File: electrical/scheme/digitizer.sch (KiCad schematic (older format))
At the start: 43 parts

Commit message: a
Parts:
- added C? (x2): 4u7, symbol C
- added C?: 3u9, symbol C
- added C? (x4): 100n, symbol C
- added R?: 100 5%, symbol R
- added R? (x2): 16 5%, symbol R
- added U?: AD7683, symbol AD7683
- added U?: MCP1703T-3302E/CB, symbol MCP1703T-3302E/CB
- added U?: AD8610, symbol AD8610
- added U?: ADG5204, symbol ADG5204
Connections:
- net labels added: adc_cs, mux-0, mux-1, src01, src02, src03, src04, vref
- wire segments 173 -> 230
- no-connect marks 5 -> 13
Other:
- moved on the sheet: C?, D?, L?, R?, U?, stm32?

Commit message: a
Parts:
- added C?: 100n, symbol C
- added C?: 1n, symbol C
- added C? (x3): 4u7, symbol C
- added C?: 10n, symbol C
- added R? (x4): 16 5%, symbol R
- added U?: MCP1703T-3302E/CB, symbol MCP1703T-3302E/CB
- R?: value 100 5% -> 50 5%
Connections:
- net labels added: adc-ref, bias-ref, in01, in02, in03, in04
- net labels removed: vref
- wire segments 230 -> 278
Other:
- moved on the sheet: C?, R?, U?

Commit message: a.
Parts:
- removed C? (x2): 100n, symbol C
- removed C? (x2): 4u7, symbol C
- removed C?: 10n, symbol C
- removed K?: swd, symbol CONN_3
- removed R? (x6): 16 5%, symbol R
- removed U?: AD8610, symbol AD8610
- removed U?: MCP1703T-3302E/CB, symbol MCP1703T-3302E/CB
- added C? (x9): 100n, symbol C
- added C? (x3): 4u7, symbol C
- added C? (x2): 1n, symbol C
- added D? (x2): LED, symbol LED
- added P?: in-0, symbol BNC
- added P?: in-1, symbol BNC
- added P?: in-2, symbol BNC
- added P?: in-3, symbol BNC
- added P?: mode, symbol CONN_01X02
- added P?: swd, symbol CONN_01X03
- added P?: ~rst~, symbol CONN_01X01
- added P?: out-0, symbol BNC
- added P?: out-1, symbol BNC
- added P?: ext, symbol CONN_01X13
- added P?: trig, symbol BNC
- added P?: trig-mode, symbol CONN_01X03
- added R? (x5): 10k 5%, symbol R
- added R?: 13k 5%, symbol R
- added R?: 1k5 5%, symbol R
- added R? (x6): 16 5%, symbol R
- added R?: 120k 5%, symbol R
- added R? (x2): 8k2 5%, symbol R
- added R? (x2): 1 5%, symbol R
- added R? (x2): 1k6 5%, symbol R
- added R? (x2): 3k3 5%, symbol R
- added R? (x2): 12k 5%, symbol R
- added R? (x3): 1k 5%, symbol R
- added U? (x6): AD8620, symbol AD8620
- added U?: MCP1703T-3302E/CB, symbol MCP1703T-3302E/CB
- added U?: BAT54S, symbol BAT54S
- C? (x2): value C -> 18p
- C?: value 3u9 -> 3n
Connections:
- net labels added: adc-mux-0, adc-mux-1, dac-cs-0, dac-cs-1, dac-cs-2, dac-cs-3, dac-mosi, dac-ref, dac-sck, gpio-0, gpio-1, gpio-2, gpio-3, gpio-4, led-0, led-1, rx-2, src-0, src-1, src-2, src-3, tx-2
- net labels removed: bias-ref, mux-0, mux-1, src01, src02, src03, src04
- wire segments 278 -> 434
- no-connect marks 13 -> 10
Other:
- note added: "To eliminate uncertanity \nif input is high Z."
- moved on the sheet: C?, R?, U?

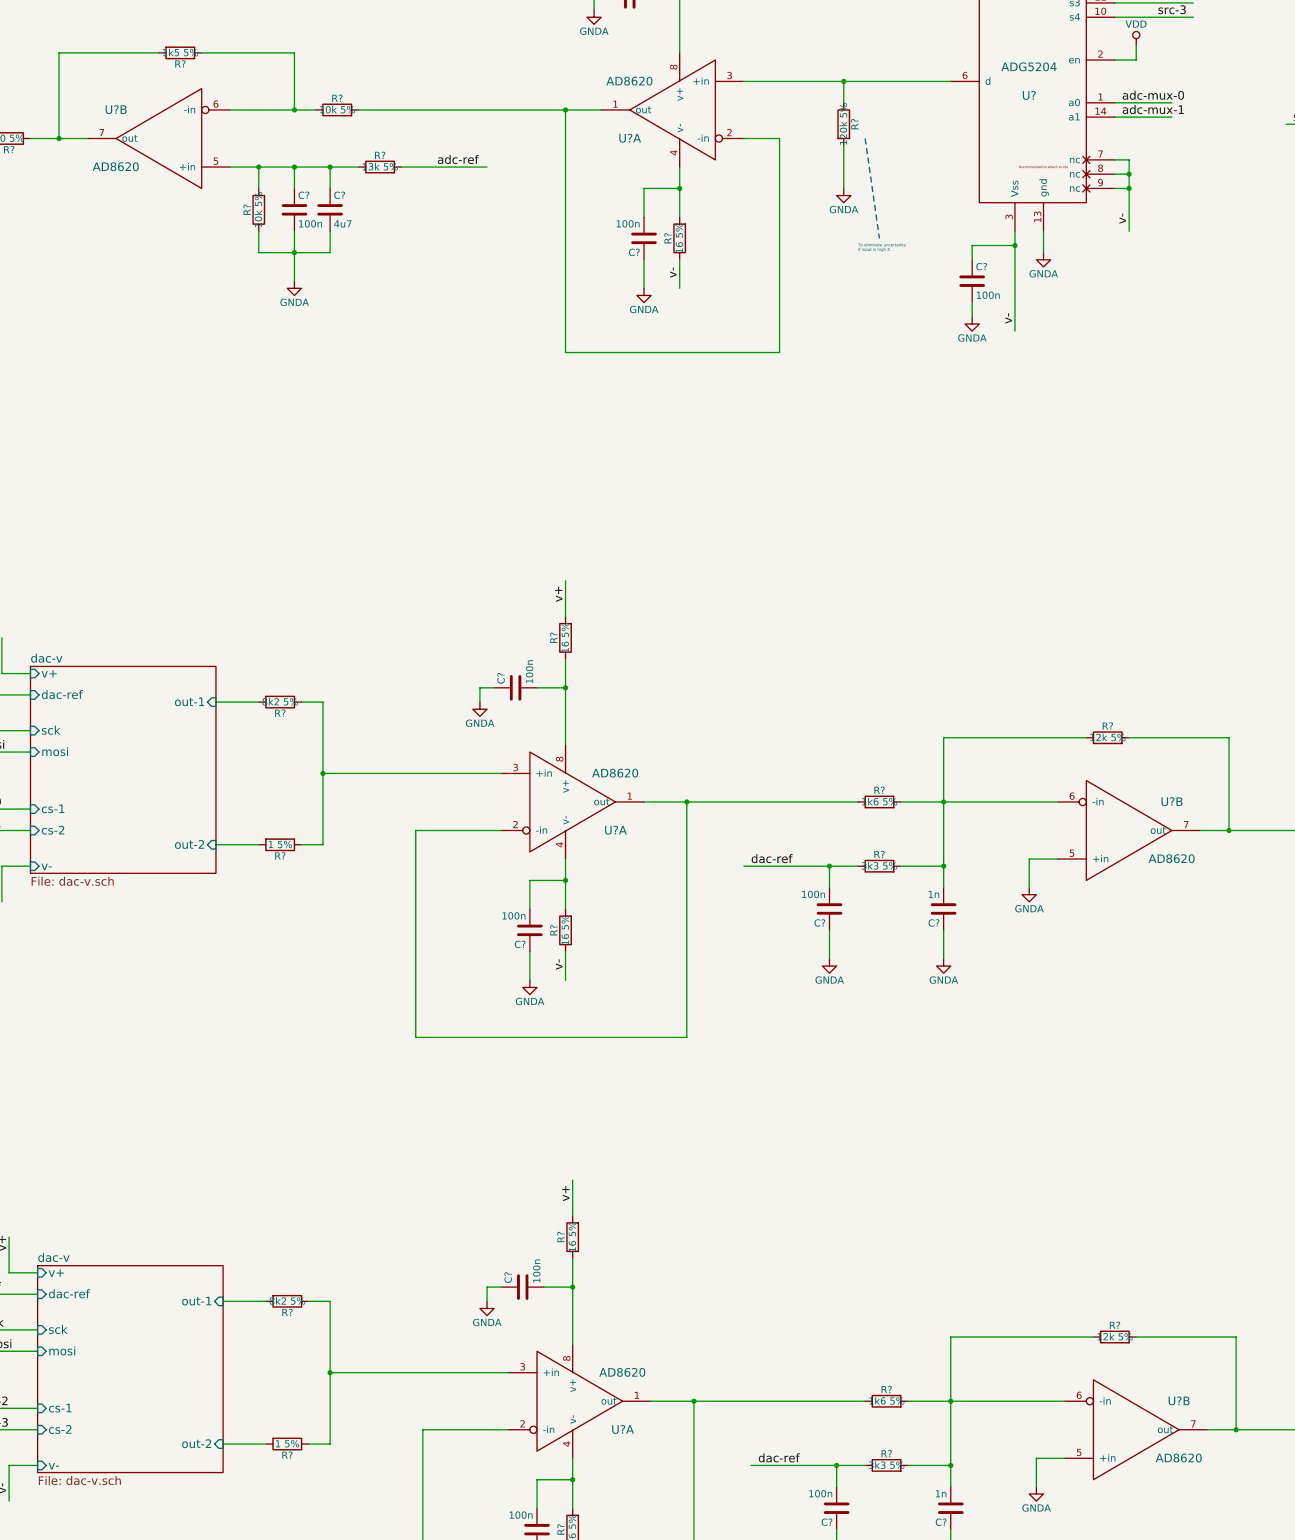
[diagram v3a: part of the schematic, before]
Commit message: Annotated opamps.
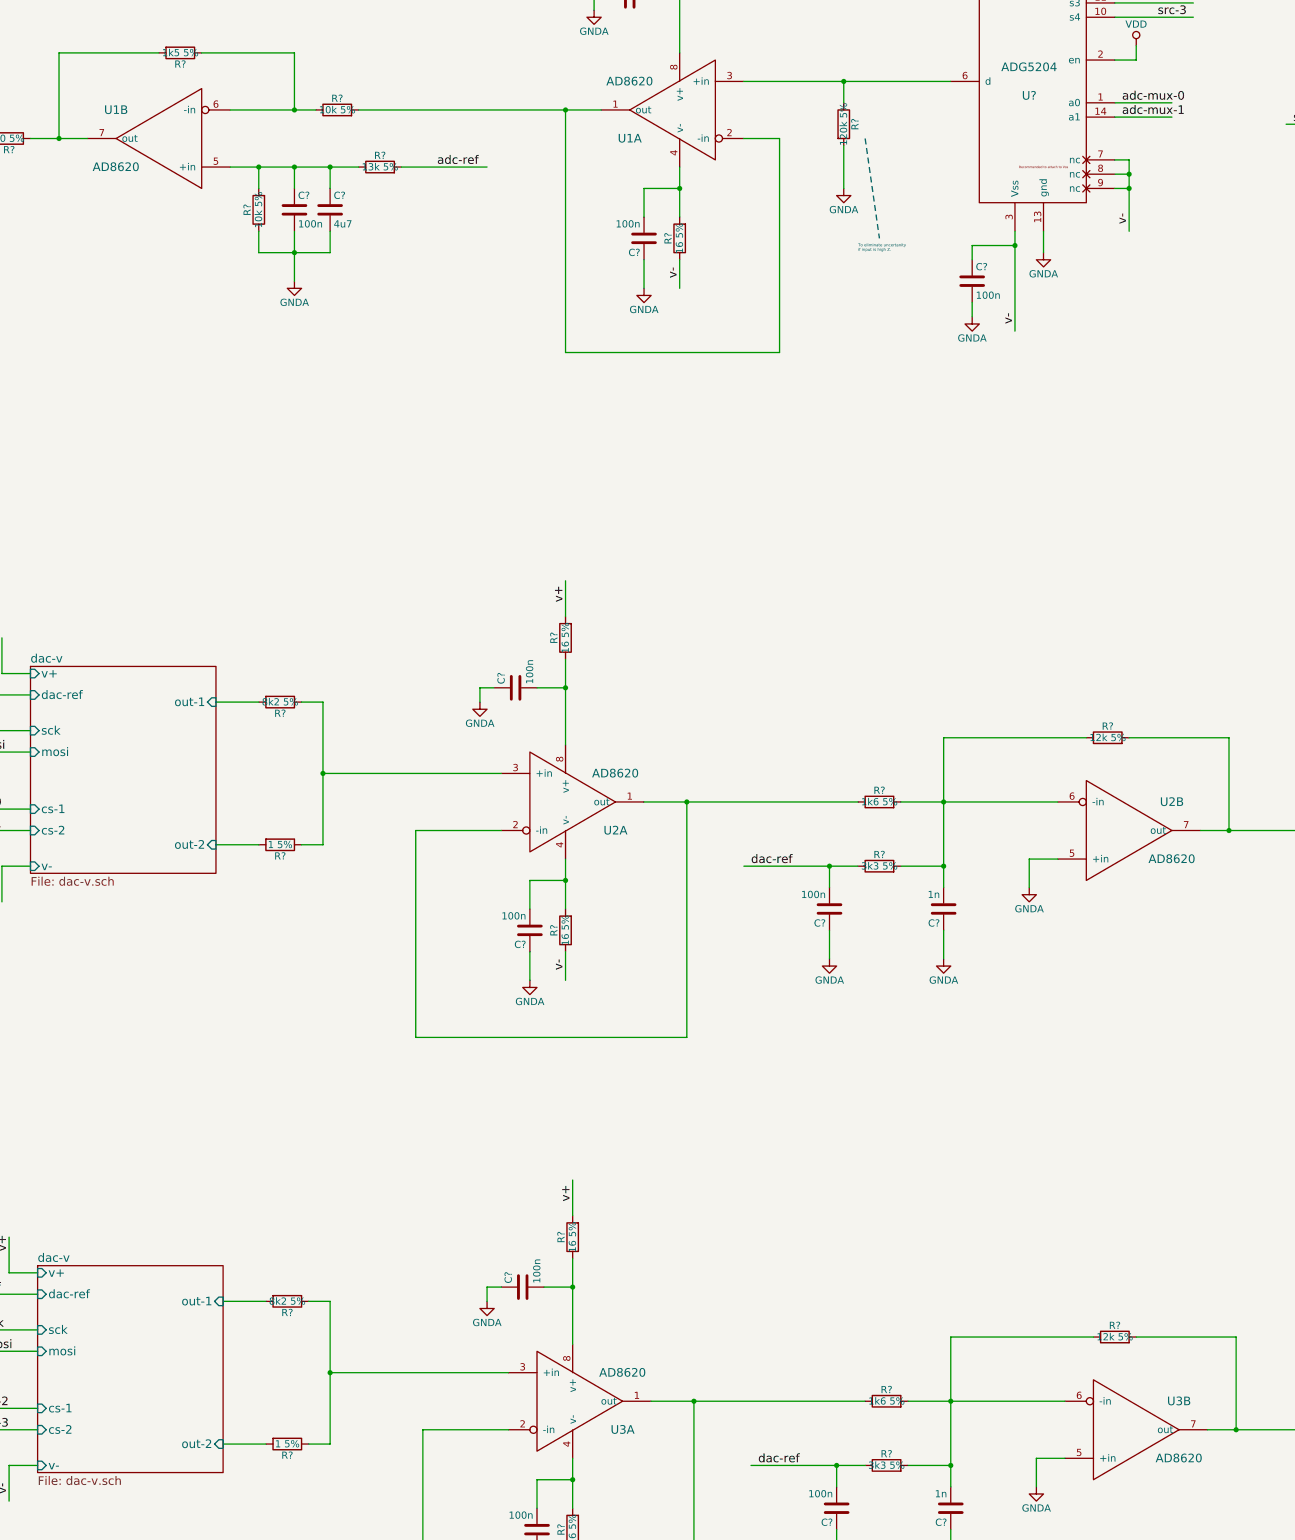
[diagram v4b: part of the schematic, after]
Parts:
- gave numbers to parts that had none: 3
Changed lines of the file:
@@
 	20300 2400 21750 2400
 $Comp
-L AD8620 U?
+L AD8620 U1
 U 1 1 5599DB58
 P 19850 2600
-F 0 "U?" H 20200 2400 60  0000 C CNN
+F 0 "U1" H 20200 2400 60  0000 C CNN
 F 1 "AD8620" H 20200 2800 60  0000 C CNN
 F 2 "" H 19900 2600 60  0000 C CNN
@@
 $EndComp
 $Comp
-L AD8620 U?
+L AD8620 U1
 U 2 1 5599DC7C
 P 16250 2800
-F 0 "U?" H 16600 2600 60  0000 C CNN
+F 0 "U1" H 16600 2600 60  0000 C CNN
 F 1 "AD8620" H 16600 3000 60  0000 C CNN
 F 2 "" H 16300 2800 60  0000 C CNN
@@
 	16900 7750 16600 7750
 $Comp
-L AD8620 U?
+L AD8620 U2
 U 1 1 55A17217
 P 19050 7450
-F 0 "U?" H 19400 7250 60  0000 C CNN
+F 0 "U2" H 19400 7250 60  0000 C CNN
 F 1 "AD8620" H 19400 7650 60  0000 C CNN
 F 2 "" H 19100 7450 60  0000 C CNN
@@
 Connection ~ 19900 7450
 $Comp
-L AD8620 U?
+L AD8620 U2
 U 2 1 55A2A22C
 P 22950 7650
-F 0 "U?" H 23300 7450 60  0000 C CNN
+F 0 "U2" H 23300 7450 60  0000 C CNN
 F 1 "AD8620" H 23300 7850 60  0000 C CNN
 F 2 "" H 23000 7650 60  0000 C CNN
@@
 	16950 11950 16650 11950
 $Comp
-L AD8620 U?
+L AD8620 U3
 U 1 1 55A5B81D
 P 19100 11650
-F 0 "U?" H 19450 11450 60  0000 C CNN
+F 0 "U3" H 19450 11450 60  0000 C CNN
 F 1 "AD8620" H 19450 11850 60  0000 C CNN
 F 2 "" H 19150 11650 60  0000 C CNN
@@
 Connection ~ 19950 11650
 $Comp
-L AD8620 U?
+L AD8620 U3
 U 2 1 55A5B860
 P 23000 11850
-F 0 "U?" H 23350 11650 60  0000 C CNN
+F 0 "U3" H 23350 11650 60  0000 C CNN
 F 1 "AD8620" H 23350 12050 60  0000 C CNN
 F 2 "" H 23050 11850 60  0000 C CNN

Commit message: a
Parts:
- removed P?: in-1, symbol BNC
- removed P?: in-2, symbol BNC
- removed P?: in-3, symbol BNC
- added C80, C81, C82, C83: 100n, Capacitors_SMD:C_0805_HandSoldering, symbol C
- added P10: in-2, Sockets_BNC:BNC_Socket_TYCO-AMP_LargePads, symbol BNC
- added P11: in-3, Sockets_BNC:BNC_Socket_TYCO-AMP_LargePads, symbol BNC
- added P12: in-1, Sockets_BNC:BNC_Socket_TYCO-AMP_LargePads, symbol BNC
- added R71, R72, R73, R74: 16 5%, Resistors_SMD:R_0805_HandSoldering, symbol R
- added U100, U101: AD8672, Housings_SOIC:SOIC-8_3.9x4.9mm_Pitch1.27mm, symbol AD8620
- C1, C10, C11, C12, C13, C14, C15, C16, C17, C18, C19, C2, C20, C21, C22, C23, C24, C25, C26, C28, C29, C3, C30, C31, C32, C33, C34, C35, C36, C37, C38, C4, C5, C6, C7, C8, C9: renamed from C?; footprint (none) -> Capacitors_SMD:C_0805_HandSoldering
- C27, C39: renamed from C?; footprint (none) -> Capacitors_ThroughHole:C_Radial_D10_L20_P5
- D1, D2: renamed from D?; footprint (none) -> LEDs:LED-3MM
- D3, D4: renamed from D?; footprint (none) -> Diodes_ThroughHole:Diode_DO-41_SOD81_Horizontal_RM10
- L1, L2: renamed from L?; footprint (none) -> my-lib:my_inductance
- P1: renamed from P?; footprint (none) -> Pin_Headers:Pin_Header_Straight_1x02
- P2: renamed from P?; footprint (none) -> Pin_Headers:Pin_Header_Straight_1x01
- P3: renamed from P?; footprint (none) -> Socket_Strips:Socket_Strip_Angled_1x13
- P4, P7, P8, P9: renamed from P?; footprint (none) -> Sockets_BNC:BNC_Socket_TYCO-AMP_LargePads
- P5: renamed from P?; footprint (none) -> Pin_Headers:Pin_Header_Angled_1x03
- P6: renamed from P?; footprint (none) -> Socket_Strips:Socket_Strip_Angled_1x03
- R1, R10, R11, R14, R15, R16, R17, R18, R19, R2, R20, R21, R22, R23, R24, R25, R26, R27, R28, R29, R3, R30, R31, R32, R33, R34, R35, R36, R37, R38, R39, R4, R40, R41, R42, R5, R6, R7, R8, R9: renamed from R?; footprint (none) -> Resistors_SMD:R_0805_HandSoldering
- R12, R13: renamed from R?; footprint ~ -> Resistors_SMD:R_0805_HandSoldering
- U1, U2, U3: value AD8620 -> AD8672; footprint (none) -> Housings_SOIC:SOIC-8_3.9x4.9mm_Pitch1.27mm
- U10: renamed from U?; footprint (none) -> crystal-smd-5x3:CRYSTAL-SMD-5x3
- U11: renamed from U?; footprint ~ -> my-lib:CP2102
- U12: renamed from U?; footprint (none) -> my-lib:my-mini-usb-b
- U13, U14, U15, U16: renamed from U?; footprint (none) -> Housings_SOT-23_SOT-143_TSOT-6:SOT-23
- U17: renamed from U?; footprint (none) -> Housings_SSOP:MSOP-8_3x3mm_Pitch0.65mm
- U18, U20: renamed from U?; footprint ~ -> Housings_SOIC:SOIC-8_3.9x4.9mm_Pitch1.27mm
- U19: renamed from U?; footprint (none) -> Housings_SSOP:TSSOP-14_4.4x5mm_Pitch0.65mm
- stm321: renamed from stm32?; footprint (none) -> my-lib:LQFP48
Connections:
- net labels added: adc-cs, adc-miso, adc-mosi, adc-sck, boot0, boot1, clk-in, clk-out, dac-miso, in-0, in-1, in-2, in-3, ~rst~
- net labels removed: Vin, adc_cs, adc_miso, adc_mosi, adc_sck, dac_miso, dac_mosi, dac_sck, in01, in02, in03, in04
- wire segments 434 -> 484
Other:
- moved on the sheet: P9

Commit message: a
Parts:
- removed U12: MINI-USB-B, my-lib:my-mini-usb-b, symbol MINI-USB-B
- added P13: USB_B, Connect:USB_B, symbol USB_B
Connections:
- wire segments 484 -> 482
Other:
- moved on the sheet: C10, C11, C12, C13, C18, C21, C23, C27, C8, C9, D3, L1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

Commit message: a
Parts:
- added C84, C86, C88, C90: 1n, Capacitors_SMD:C_0805_HandSoldering, symbol C
- added C85, C87, C89, C91: 680u, Capacitors_ThroughHole:C_Radial_D10_L20_P5, symbol CP
- added C? (x4): 100n, Capacitors_SMD:C_0805_HandSoldering, symbol C
- added C?: 4u7, Capacitors_SMD:C_0805_HandSoldering, symbol C
- added L3, L4, L5, L6: 100uH, my-lib:my_inductance, symbol INDUCTOR
- C27, C39: value 330u -> 680u
- L1: value 50uH -> 100uH
- P1: footprint Pin_Headers:Pin_Header_Straight_1x02 -> Pin_Headers:Pin_Header_Angled_1x02
- P6: footprint Socket_Strips:Socket_Strip_Angled_1x03 -> Socket_Strips:Socket_Strip_Straight_1x03
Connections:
- wire segments 482 -> 515
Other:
- moved on the sheet: C36, C37, C38, C39, D4, L2, R38, R39, R42, U20

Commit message: a
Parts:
- added C97, C98: 4u7, Capacitors_SMD:C_0805_HandSoldering, symbol C
- added L7, L8: 47uH, Capacitors_SMD:C_1206_HandSoldering, symbol INDUCTOR
- R10, R8: value 10k 5% -> 33k 5%
- gave numbers to parts that had none: 5
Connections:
- wire segments 515 -> 521
